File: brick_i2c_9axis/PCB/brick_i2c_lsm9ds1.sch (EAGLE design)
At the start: 11 parts

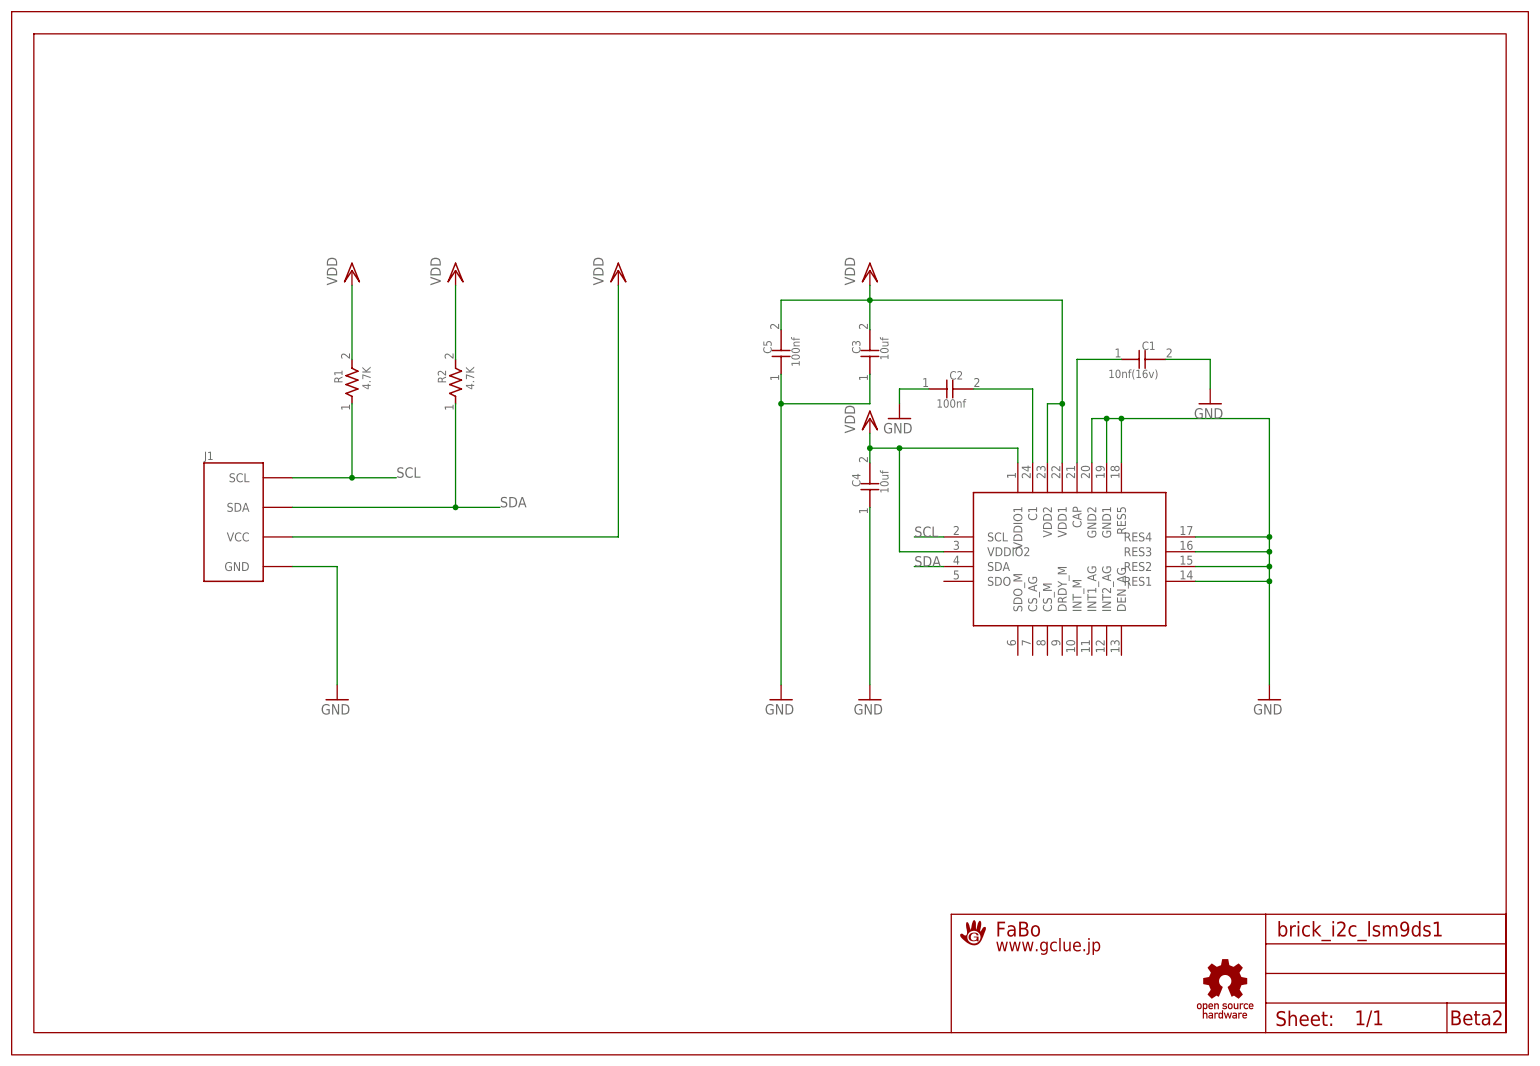
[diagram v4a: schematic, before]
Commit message: change logo
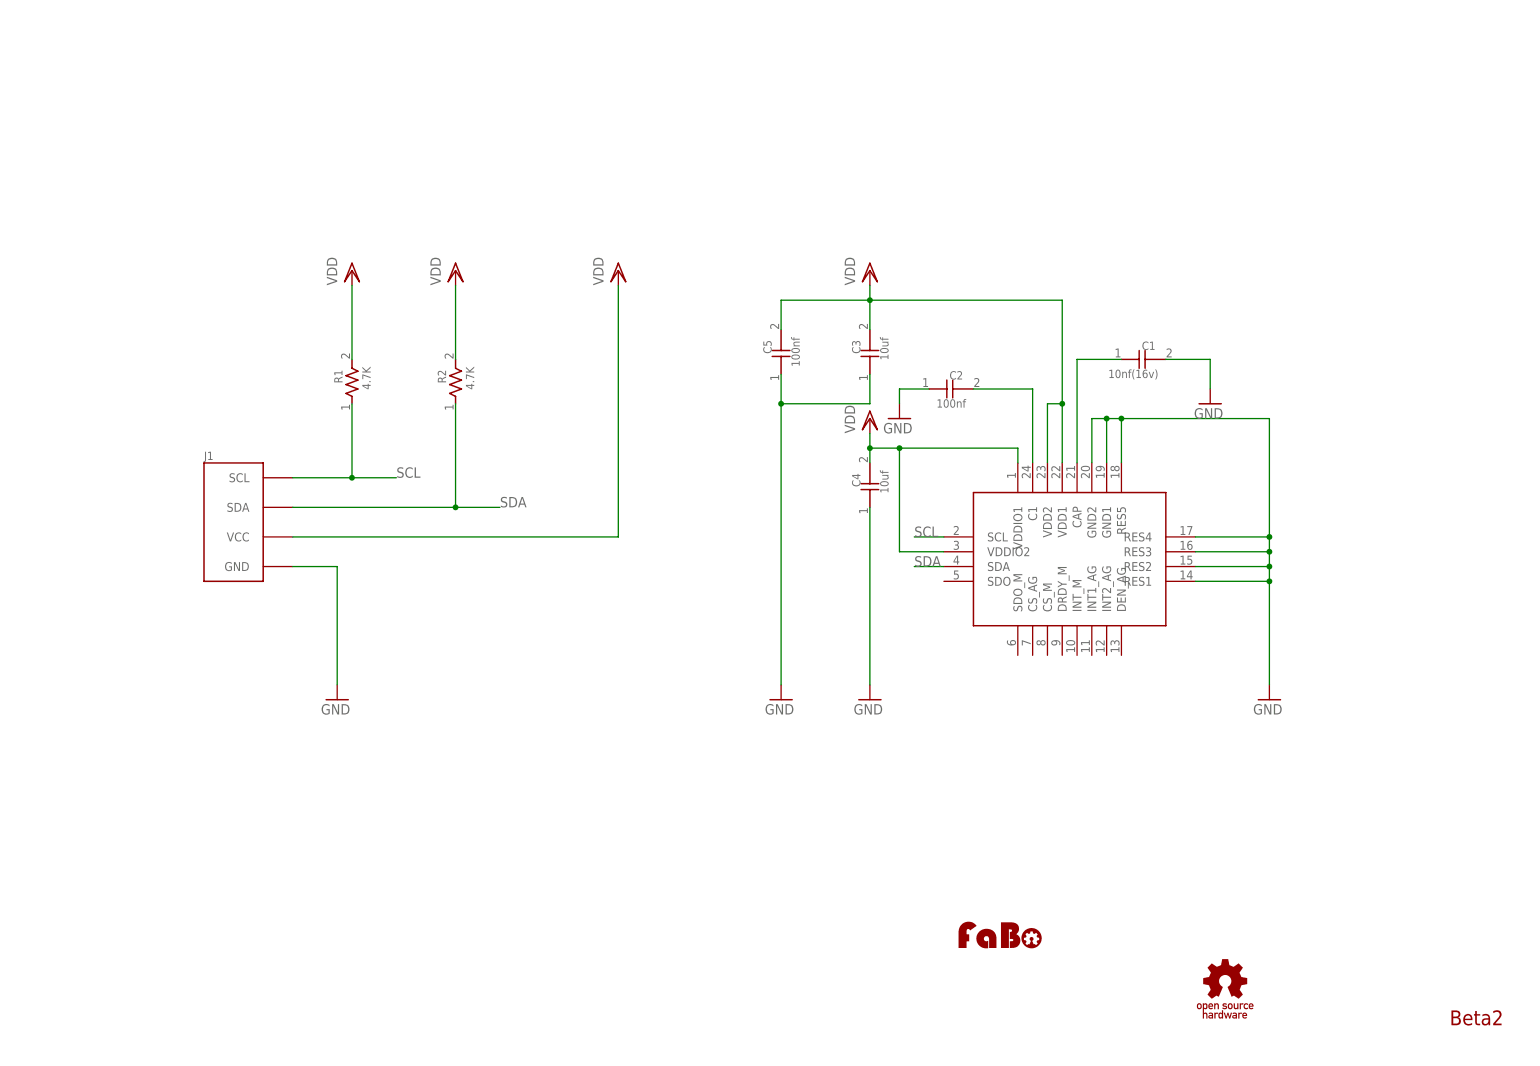
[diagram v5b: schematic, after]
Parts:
- removed U$2: A4L-LOC-FABO_M, gclue:A4L-LOC-FABO_M
- added U$4: (no value), FaBo:LOGO_FABO-M
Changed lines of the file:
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@@
 </classes>
 <parts>
-<part name="U$2" library="gclue" deviceset="A4L-LOC" device="-FABO_M"/>
+<part name="U$2" library="gclue" deviceset="A4L-LOC" device=""/>
 <part name="GND9" library="gclue" deviceset="GND" device=""/>
 <part name="GND10" library="gclue" deviceset="GND" device=""/>
@@
 <part name="J1" library="gclue" deviceset="BRICK_I2C" device=""/>
 <part name="U$3" library="gclue" deviceset="LOGO_OSHW_T" device="-M"/>
+<part name="U$4" library="FaBo" deviceset="LOGO_FABO" device="-M"/>
 </parts>
 <sheets>
@@
 <instance part="J1" gate="G$1" x="43.18" y="91.44"/>
 <instance part="U$3" gate="G$1" x="210.82" y="12.7"/>
+<instance part="U$4" gate="G$1" x="165.1" y="22.86"/>
 </instances>
 <busses>
